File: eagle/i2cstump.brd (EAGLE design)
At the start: 31.2 x 19 mm, 22 parts, among them IC1 ATTINY85, IC2 MCP1703CB, J1 I2C-5V, J2 I2C-3V3, J3 AVR_SPI_PROG_3X2TESTPOINTS, Q1 220mA/50V/3.5Ω, Q2 220mA/50V/3.5Ω, X1 USBPCB

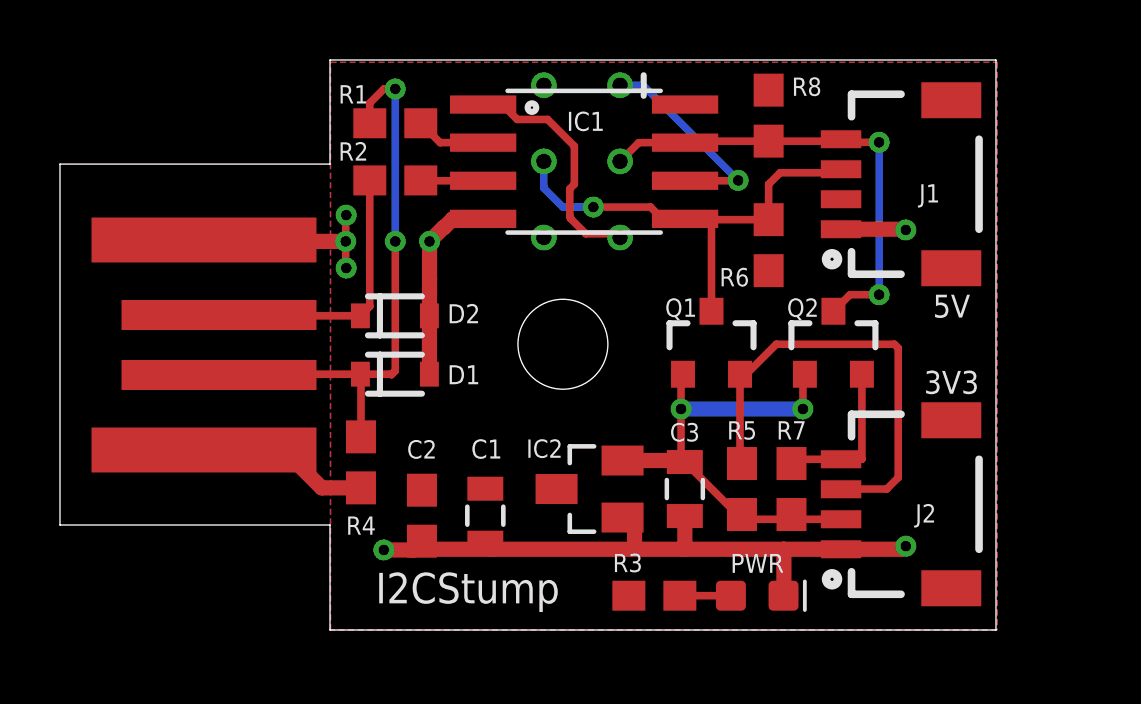
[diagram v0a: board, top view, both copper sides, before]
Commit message: Version 4.0
Changes:
- swap out PWR led for ACT led on MISO pin (the USB Tiny I2C firmware
blinks MISO on I2C activity.
- swap out 10KOhm pullup resistors for an 0805 resistor network RN1.
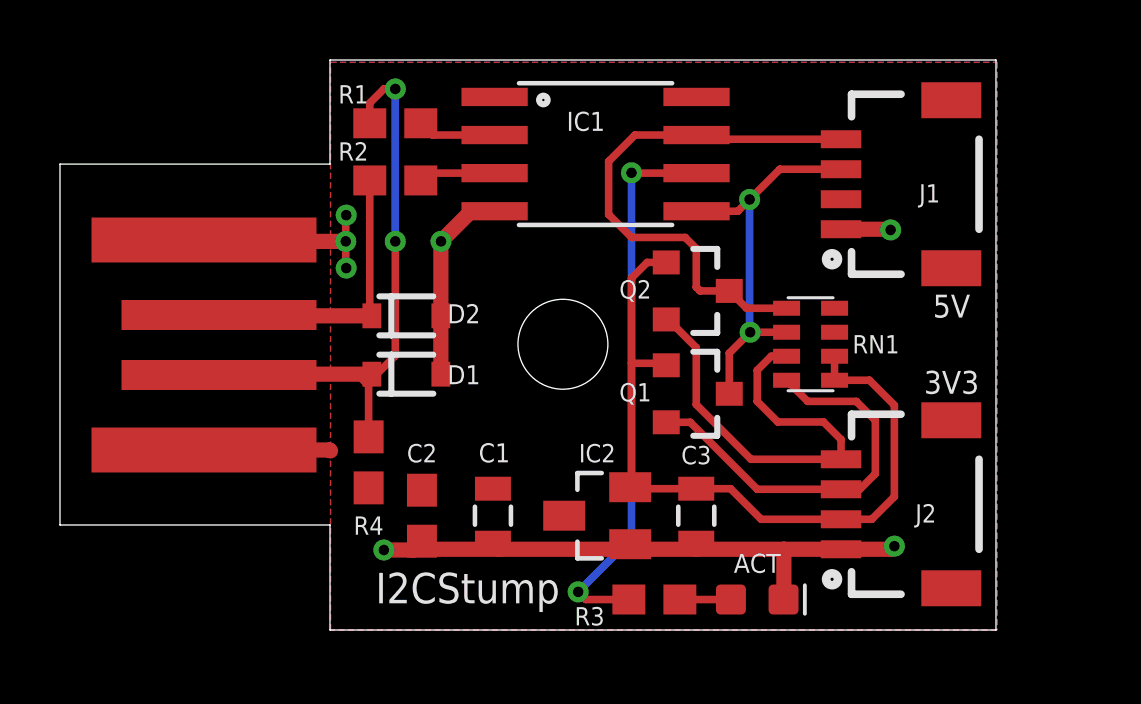
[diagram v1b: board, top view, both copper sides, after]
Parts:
- removed J3: AVR_SPI_PROG_3X2TESTPOINTS, SparkFun-Connectors:2X3_TEST_POINTS
- removed R5, R6, R7, R8: 10k, SparkFun-Resistors:0603
- added RN1: CTS742C083, resistor-net:CTS742C083
- moved Q2 4.91 mm to (21.2, 11.3), turned to 270 degrees
- moved Q1 1.73 mm to (21.2, 7.87), turned to 270 degrees
- moved C3 0.97 mm to (21.2, 3.81)
- moved IC2 0.92 mm to (17.9, 3.81)
- moved IC1 0.46 mm to (17.9, 15.9)
- moved D1 0.38 mm to (11.5, 8.53)
- moved D2 0.38 mm to (11.5, 10.5)
- moved R4 0.25 mm to (10.3, 5.59)
- moved C1 0.25 mm to (14.4, 3.81)
- moved D3 0.13 mm to (23.2, 1.02)
- moved R3 0.13 mm to (19.8, 1.02)
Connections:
- net +3V3: now also RN1.5, RN1.6; no longer R5.2, R7.2
- net 5V: now also RN1.7, RN1.8; no longer J3.2, R3.2, R6.2, R8.2
- net GND: no longer J3.6
- net MISO: now also R3.2; no longer J3.1
- net RST: no longer J3.5
- net SCL: now also RN1.1; no longer J3.3, R8.1
- net SCL33: now also RN1.3; no longer R7.1
- net SDA: now also RN1.2; no longer J3.4, R6.1
- net SDA33: now also RN1.4; no longer R5.1
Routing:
- net MISO: track 7.03 -> 18.8 mm, vias 1 -> 2
- net SCL33: track 5.24 -> 15.1 mm
- net +3V3: track 16.4 -> 25.3 mm, vias 2 -> 0
- net RST: track 8.01 -> 0.00 mm
- net GND: track 37.1 -> 34.6 mm
- net SDA: track 15.7 -> 13.4 mm, vias 1 -> 2
- net SCL: track 15.8 -> 17.9 mm, vias 2 -> 0
- net 5V: track 6.10 -> 4.23 mm
- net SDA33: track 15.1 -> 13.4 mm
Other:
- board text added: "ACT"
- board text added: "RN1"
- board text added: "github.com/pimvanpelt/i2cstump I2C, 3.3V & 5V Version 4.0"
- board text removed: "CLK"
- board text removed: "ICSP"
- board text removed: "MISO"
- board text removed: "MOSI"
- board text removed: "PWR"
- board text removed: "RST"
- board text removed: "github.com/pimvanpelt/i2cstump I2C, 3.3V & 5V Version 3.0"

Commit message: Add a few mm of length to the USB stump
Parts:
- moved C1 2.81 mm to (17.2, 3.56)
- moved C2 2.81 mm to (14.9, 3.56)
- moved C3 2.81 mm to (24.0, 3.56)
- moved D3 2.81 mm to (26.0, 0.76)
- moved IC1 2.81 mm to (20.7, 15.6)
- moved IC2 2.81 mm to (20.7, 3.56)
- moved J1 2.81 mm to (28.8, 14.6)
- moved J2 2.81 mm to (28.8, 3.94)
- moved Q1 2.81 mm to (24.0, 7.62)
- moved Q2 2.81 mm to (24.0, 11.0)
- moved R2 2.81 mm to (14.0, 14.7)
- moved R3 2.81 mm to (22.6, 0.76)
- moved RN1 2.81 mm to (27.8, 9.27)
- moved R1 2.81 mm to (14.0, 16.6)
- moved D1 2.81 mm to (14.3, 8.27)
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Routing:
- net USB_M: track 19.5 -> 22.2 mm
- net GND: track 34.6 -> 37.3 mm
- net 5V: track 4.23 -> 6.90 mm
- net USB_P: track 9.65 -> 12.3 mm
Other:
- board size 31.2 x 19 mm -> 34 x 19 mm
- board text added: "github.com/pimvanpelt/i2cstump I2C, 3.3V & 5V Version 4.1"
- board text removed: "github.com/pimvanpelt/i2cstump I2C, 3.3V & 5V Version 4.0"
